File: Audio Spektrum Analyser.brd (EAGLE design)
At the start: 227.3 x 136.8 mm, 145 parts, among them IC1 LM324N, IC10 LM3914N, IC11 LM3914N, IC12 LM3914N, IC13 LM3914N, IC2 LM324N, IC3 LM324N, IC4 LM3914N, IC5 LM3914N, IC6 LM3914N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

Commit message: created final shape
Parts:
- R16: value 1M -> 22k
- moved R37 68.7 mm to (127.0, 26.7)
- moved R16 64.3 mm to (102.9, 16.5), flipped to the bottom, turned to 0 degrees
- moved TP1 63.5 mm to (43.2, -17.8)
- moved D11 57.2 mm to (135.9, 34.3)
- moved C11 57.2 mm to (29.2, 38.1)
- moved C20 57.2 mm to (43.2, 38.1)
- moved C21 57.2 mm to (57.1, 38.1)
- moved C43 57.2 mm to (92.7, 39.4)
- moved D4 57.2 mm to (52.1, 34.3)
- moved IC10 57.2 mm to (92.7, 53.3)
- moved C10 57.1 mm to (15.2, 38.1)
- moved C22 57.1 mm to (71.1, 38.1)
- moved C23 57.1 mm to (85.1, 38.1)
- moved C32 57.1 mm to (99.1, 38.1)
- moved C33 57.1 mm to (113.0, 38.1)
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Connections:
- removed net N$124: IC1.5
- net N$3: now also IC1.5
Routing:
- net VER: track 0.00 -> 168.4 mm
- net +5V: track 459.2 -> 606.1 mm
- net REF: track 0.00 -> 140.0 mm
- net N$144: track 13.2 -> 75.5 mm
- net N$4: track 0.00 -> 58.3 mm
- net N$125: track 13.2 -> 70.2 mm
- net N$133: track 13.2 -> 69.2 mm
- net N$159: track 13.2 -> 55.3 mm
- net N$151: track 13.2 -> 53.0 mm
- net N$149: track 13.2 -> 52.7 mm
- net N$3: track 0.00 -> 37.7 mm
- net N$163: track 13.2 -> 37.4 mm
- net N$12: track 0.00 -> 23.8 mm
- net N$167: track 13.2 -> 36.2 mm
- net N$10: track 0.00 -> 20.4 mm
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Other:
- board size 227.3 x 136.8 mm -> 144.8 x 98.7 mm

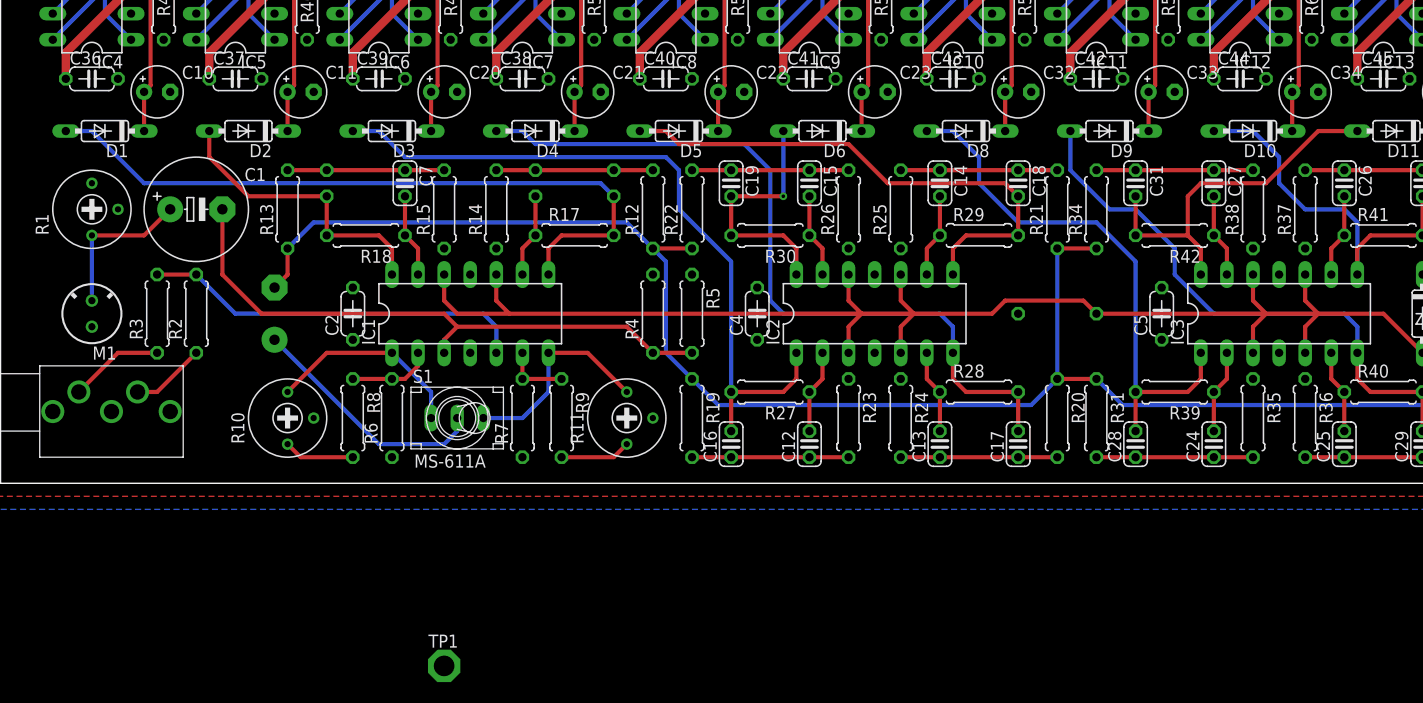
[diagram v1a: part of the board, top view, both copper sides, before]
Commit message: moved caps and co to top side
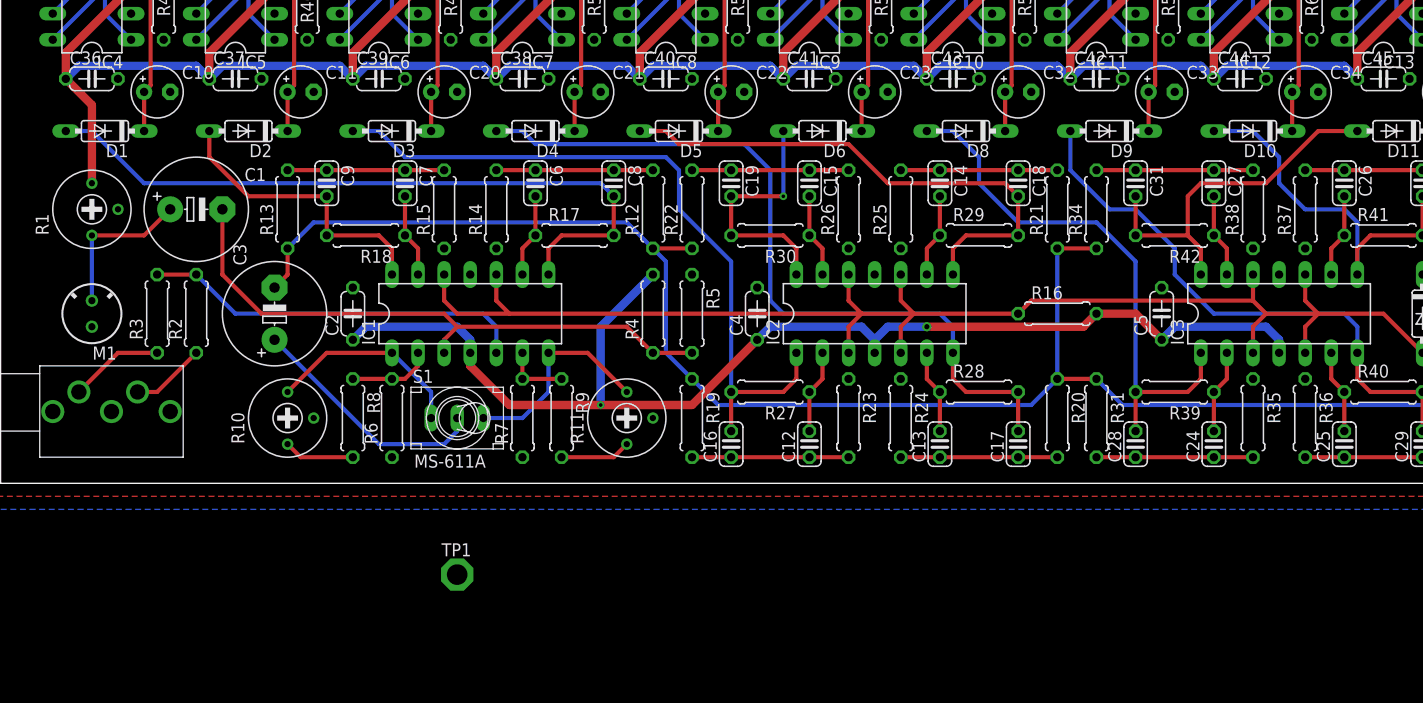
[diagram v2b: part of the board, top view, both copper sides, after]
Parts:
- moved TP1 8.98 mm to (44.5, -8.89)
- flipped C3 to the top
- flipped C6 to the top
- flipped C8 to the top
- flipped C9 to the top
- flipped R16 to the top
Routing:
- net +5V: track 606.1 -> 872.1 mm, vias 0 -> 2
- net REF: track 140.0 -> 138.2 mm

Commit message: replaced dc blocking caps, print back side, added dc jack
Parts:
- added J2: DCJ0202, con-jack:DCJ0202
- C1, C3: value 100u -> 2u2; device resistor:E5-10,5 -> resistor:E2,5-5
- R1, R10, R11: device resistor:RTRIM3339P -> pot:CA6V
- moved M1 13.1 mm to (15.2, 27.9)
- moved J1 11.4 mm to (3.81, 22.9)
- moved R3 10.2 mm to (20.3, 7.62)
- moved C1 4.02 mm to (22.9, 25.4), turned to 270 degrees
- moved R1 2.84 mm to (6.35, 27.9), turned to 180 degrees
- moved C3 2.84 mm to (29.2, 17.8)
- moved R2 1.80 mm to (20.3, 17.8), turned to 270 degrees
- turned R10 to 180 degrees
- turned R11 to 180 degrees
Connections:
- net +5V: now also J2.1, R1.E; no longer R1.3
- net GND: now also J2.3
- net N$10: now also R11.E; no longer R11.3
- net N$13: now also R1.S; no longer R1.1
- net N$31: now also R10.S; no longer R10.1
- net N$44: now also R11.S; no longer R11.1
- net N$6: now also R10.E; no longer R10.3
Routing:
- net +5V: track 872.1 -> 926.1 mm
- net N$2: track 9.20 -> 21.8 mm
- net N$13: track 15.0 -> 19.1 mm
- net N$4: track 58.3 -> 54.5 mm
- net N$6: track 19.7 -> 22.2 mm
- net N$3: track 37.7 -> 35.7 mm
- net N$10: track 20.4 -> 19.4 mm
- net N$12: track 23.8 -> 24.5 mm
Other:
- board text added: "1 kHz"
- board text added: "128 Hz"
- board text added: "16 kHz"
- board text added: "2 kHz"
- board text added: "256 Hz"
- board text added: "32 Hz"
- board text added: "4 kHz"
- board text added: "512 Hz"
- board text added: "5V"
- board text added: "64 Hz"
- board text added: "8 kHz"
- board text added: ">VERSION"
- board text added: "Audio Spektrum Analyzer"
- board text added: "von Jakob Holz"

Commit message: updated to eagle 9.1.1
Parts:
- added TP2, TP3: TPPAD1-20, testpad:P1-20
- moved TP1 31.2 mm to (58.4, 19.1)
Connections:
- net +5V: now also TP3.TP
- net GND: now also TP2.TP
- net N$12: no longer TP1.TP
- net VER: now also TP1.TP
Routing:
- net +5V: track 926.1 -> 936.1 mm
- net VER: track 168.4 -> 176.1 mm
